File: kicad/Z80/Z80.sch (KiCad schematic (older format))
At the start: 1 part

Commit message: KiCAD Z80 testing
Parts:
- added C? (x2): C_Small, symbol Device:C_Small
- added D? (x3): LED, symbol Device:LED
- added R?: R_Small, symbol Device:R_Small
- added R? (x11): 470, symbol Device:R_Small
- added U?: HEF4093B, symbol 4xxx:HEF4093B
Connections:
- net at U?.10 (D6): now also R?.1
- net VCC: now reaches U?.11 (VCC)
- net VCC: now also C?.2
- net at U?.12 (D2): now also R?.1
- net at U?.13 (D7): now also R?.1
- net at U?.14 (D0): now also R?.1
- net at U?.15 (D1): now also R?.1
- net GND: now reaches U?.29 (GND)
- net GND: now also C?.1, C?.2, D?.1 (K), D?.1 (K), D?.1 (K), R?.2, R?.2, R?.2, R?.2, R?.2, R?.2, R?.2, R?.2
- net at U?.30 (A0): now also R?.1
- net at U?.31 (A1): now also R?.1
- net at U?.32 (A2): now also R?.1
- net CLK: now reaches U?.6 (~CLK~)
- net CLK: now also R?.1, U?.3
- net at U?.7 (D4): now also R?.1
- net at U?.8 (D3): now also R?.1
- net at U?.9 (D5): now also R?.1
- new net: C?.1, R?.2, U?.1, U?.2
- new net: D?.2 (A), R?.2 (x3)
- no-connect marks 0 -> 13
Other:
- moved on the sheet: U?

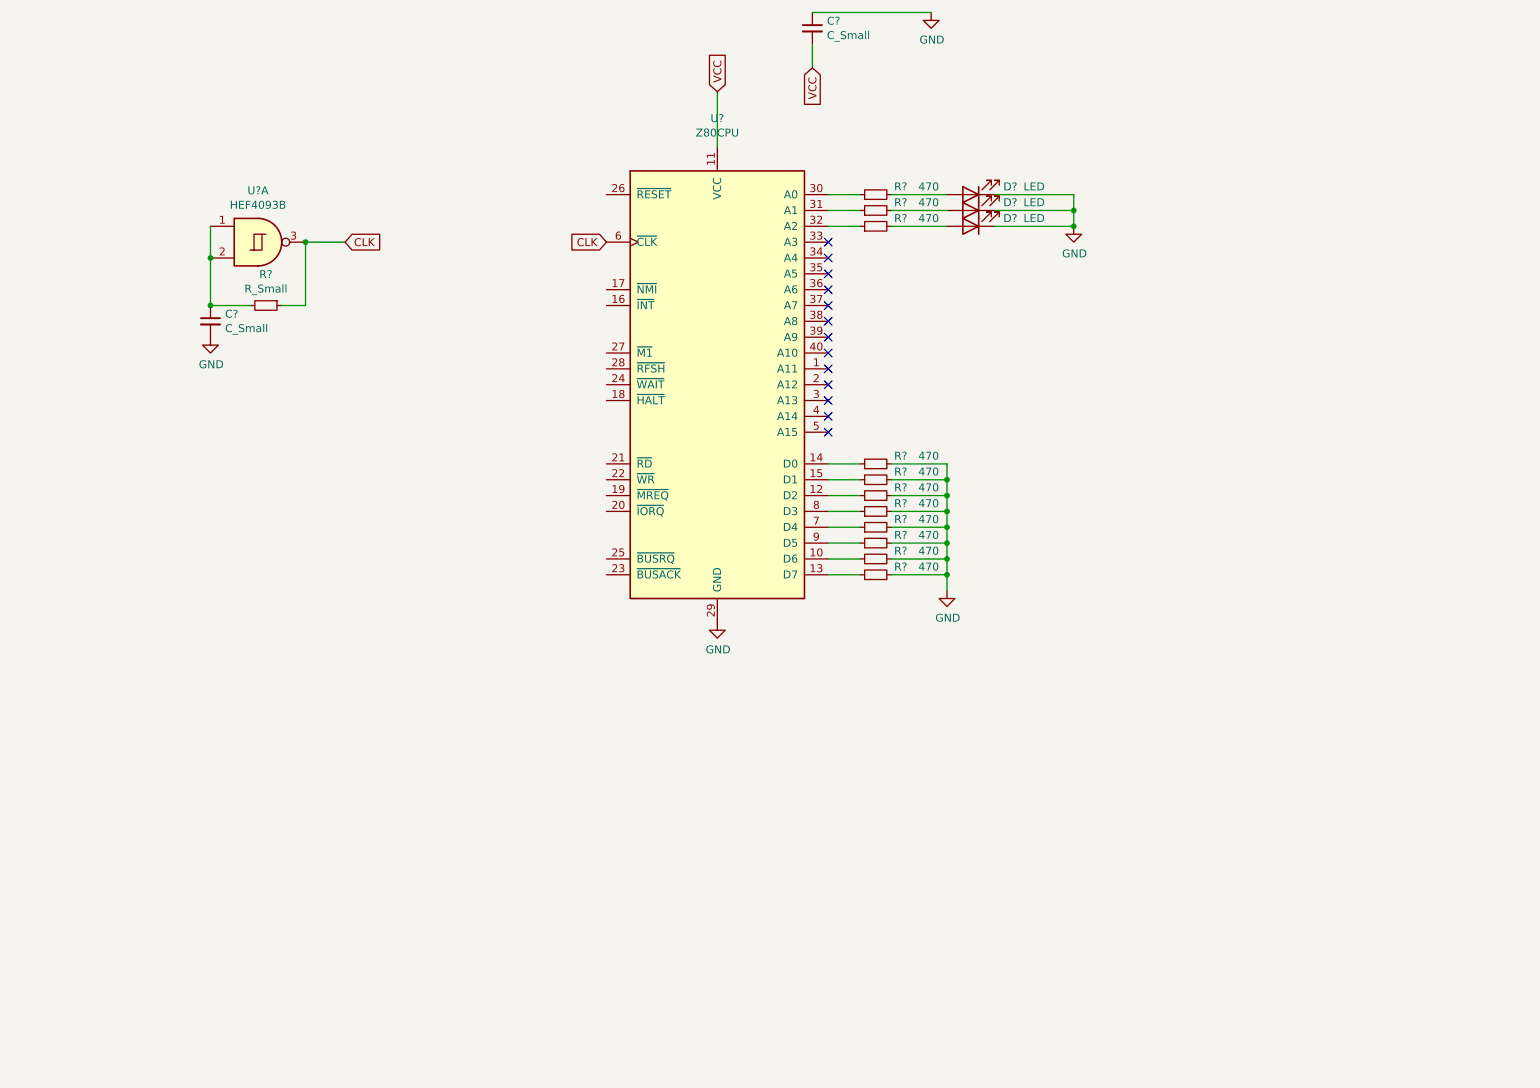
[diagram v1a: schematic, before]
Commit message: Z80 tester complete
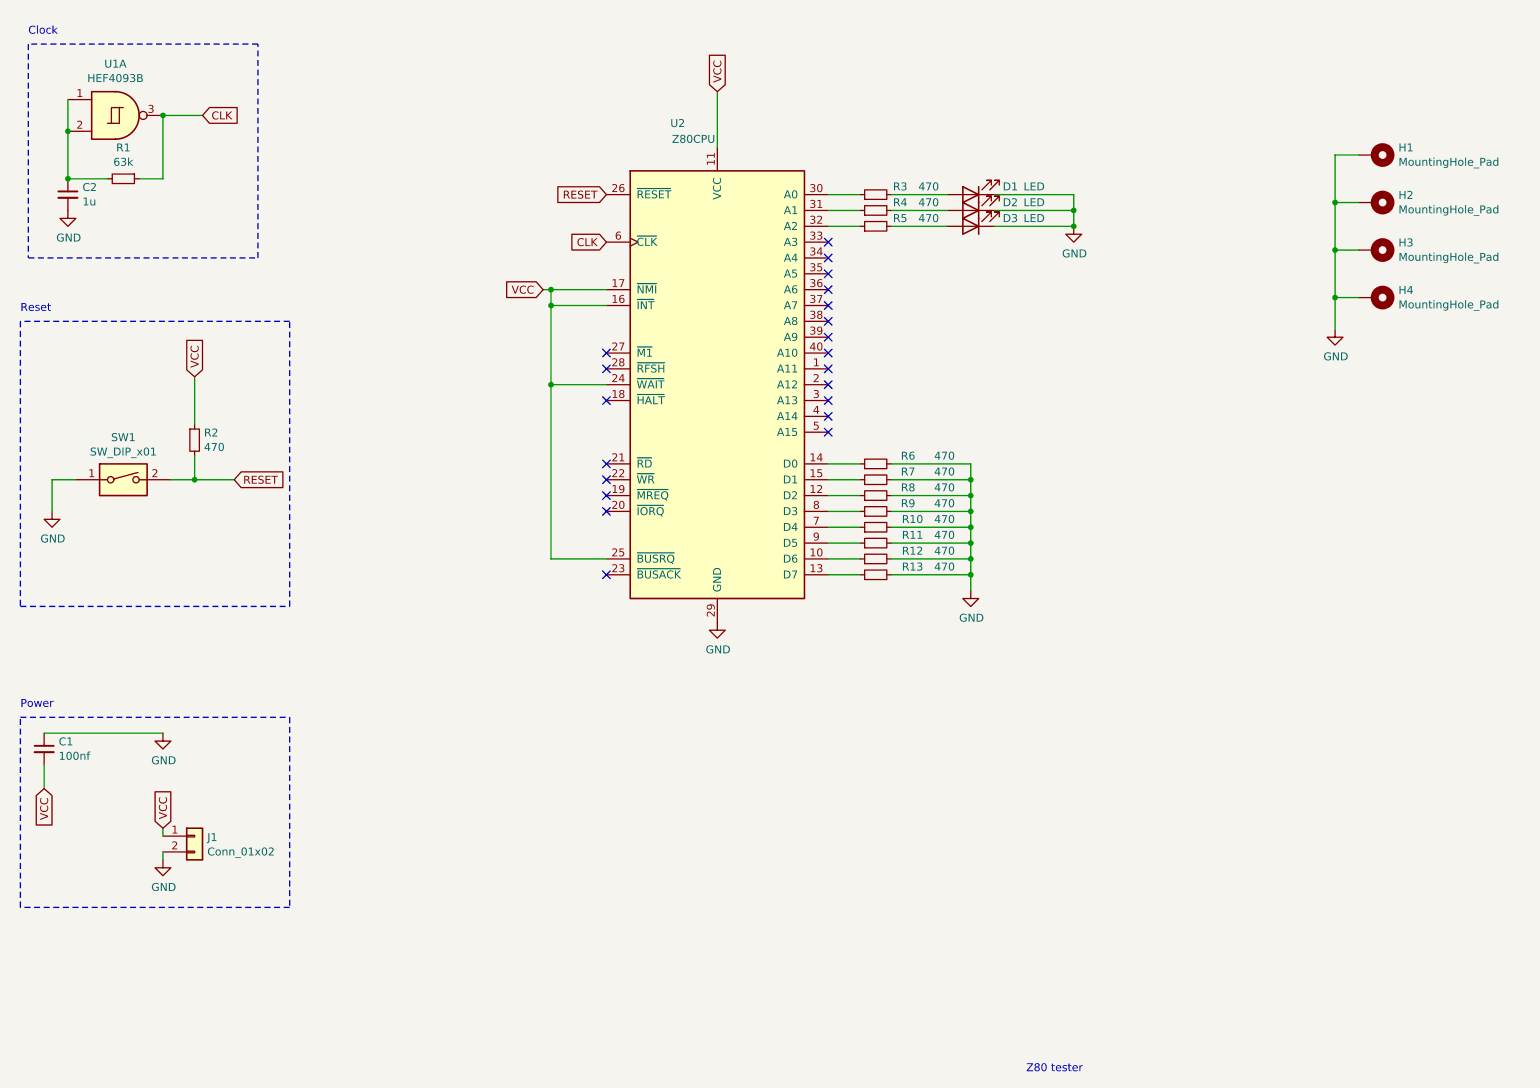
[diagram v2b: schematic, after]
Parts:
- added H1, H2, H3, H4: MountingHole_Pad, MountingHole:MountingHole_4.3mm_M4_Pad_Via, symbol Mechanical:MountingHole_Pad
- added J1: Conn_01x02, Connector_PinHeader_2.54mm:PinHeader_1x02_P2.54mm_Vertical, symbol Connector_Generic:Conn_01x02
- added R2: 470, Resistor_SMD:R_0805_2012Metric, symbol Device:R_Small
- added SW1: SW_DIP_x01, Button_Switch_SMD:SW_SPST_EVPBF, symbol Switch:SW_DIP_x01
- C1: renamed from C?; value C_Small -> 100nf; footprint (none) -> Capacitor_SMD:C_0805_2012Metric
- C2: renamed from C?; value C_Small -> 1u; footprint (none) -> Capacitor_SMD:C_0402_1005Metric
- D1, D2, D3: renamed from D?; footprint (none) -> LED_SMD:LED_0805_2012Metric
- R1: renamed from R?; value R_Small -> 63k; footprint (none) -> Resistor_SMD:R_0805_2012Metric
- R10, R11, R12, R13, R3, R4, R5, R6, R7, R8, R9: renamed from R?; footprint (none) -> Resistor_SMD:R_0805_2012Metric
- U1: renamed from U?; footprint (none) -> Package_DIP:DIP-14_W7.62mm_Socket
- U2: renamed from U?; footprint (none) -> Package_DIP:DIP-40_W15.24mm_Socket
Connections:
- net GND: now also H1.1, H2.1, H3.1, H4.1, J1.2 (Pin_2), SW1.1
- net VCC: now also U2.16 (~INT~), U2.17 (~NMI~), U2.24 (~WAIT~), U2.25 (~BUSRQ~), J1.1 (Pin_1), R2.1
- net RESET: now reaches U2.26 (~RESET~)
- net RESET: now also R2.2, SW1.2
- no-connect marks 13 -> 21
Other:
- note added: "Clock"
- note added: "Power"
- note added: "Reset"
- note added: "Z80 tester"
- moved on the sheet: C1, C2, R1, U1A

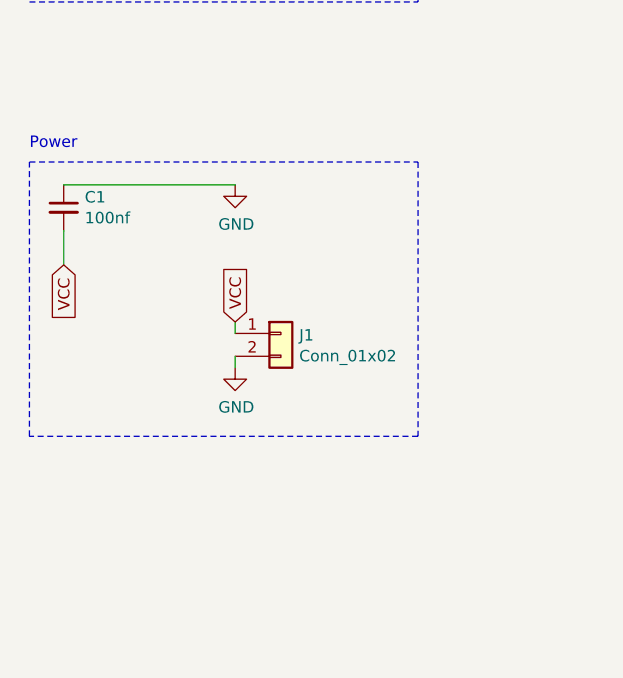
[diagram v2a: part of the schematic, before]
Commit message: add FPGA
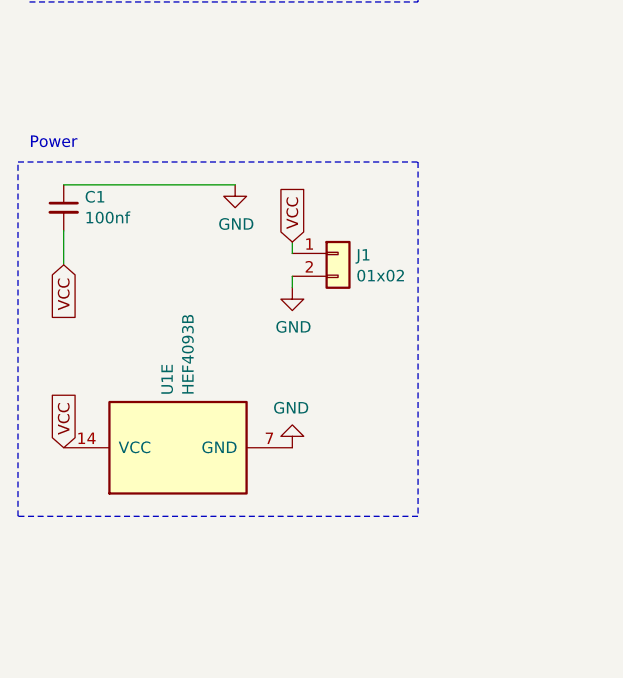
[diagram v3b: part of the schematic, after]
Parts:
- added unit 5 of U1
- C2: footprint Capacitor_SMD:C_0402_1005Metric -> Capacitor_SMD:C_0805_2012Metric
- D1, D2, D3: footprint LED_SMD:LED_0805_2012Metric -> LED_THT:LED_D5.0mm_Clear
- J1: value Conn_01x02 -> 01x02
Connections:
- net GND: now also U1.7 (GND)
- net VCC: now also U1.14 (VCC)
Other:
- moved on the sheet: J1
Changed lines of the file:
@@
 F 0 "C2" H 1442 1996 50  0000 L CNN
 F 1 "1u" H 1442 1905 50  0000 L CNN
-F 2 "Capacitor_SMD:C_0402_1005Metric" H 1350 1950 50  0001 C CNN
+F 2 "Capacitor_SMD:C_0805_2012Metric" H 1350 1950 50  0001 C CNN
 F 3 "~" H 1350 1950 50  0001 C CNN
 	1    1350 1950
@@
 F 0 "D1" H 6800 1900 50  0000 C CNN
 F 1 "LED" H 6650 1900 50  0000 C CNN
-F 2 "LED_SMD:LED_0805_2012Metric" H 7050 1950 50  0001 C CNN
+F 2 "LED_THT:LED_D5.0mm_Clear" H 7050 1950 50  0001 C CNN
 F 3 "~" H 7050 1950 50  0001 C CNN
 	1    7050 1950
@@
 F 0 "D2" H 6800 2000 50  0000 C CNN
 F 1 "LED" H 6650 2000 50  0000 C CNN
-F 2 "LED_SMD:LED_0805_2012Metric" H 7050 2050 50  0001 C CNN
+F 2 "LED_THT:LED_D5.0mm_Clear" H 7050 2050 50  0001 C CNN
 F 3 "~" H 7050 2050 50  0001 C CNN
 	1    7050 2050
@@
 F 0 "D3" H 6800 2100 50  0000 C CNN
 F 1 "LED" H 6650 2100 50  0000 C CNN
-F 2 "LED_SMD:LED_0805_2012Metric" H 7050 2150 50  0001 C CNN
+F 2 "LED_THT:LED_D5.0mm_Clear" H 7050 2150 50  0001 C CNN
 F 3 "~" H 7050 2150 50  0001 C CNN
 	1    7050 2150
@@
 L Connector_Generic:Conn_01x02 J1
 U 1 1 5EE08694
-P 2150 6000
-F 0 "J1" H 2230 5992 50  0000 L CNN
-F 1 "Conn_01x02" H 2230 5901 50  0000 L CNN
-F 2 "Connector_PinHeader_2.54mm:PinHeader_1x02_P2.54mm_Vertical" H 2150 6000 50  0001 C CNN
-F 3 "~" H 2150 6000 50  0001 C CNN
-	1    2150 6000
+P 2400 5650
+F 0 "J1" H 2480 5642 50  0000 L CNN
+F 1 "01x02" H 2480 5551 50  0000 L CNN
+F 2 "Connector_PinHeader_2.54mm:PinHeader_1x02_P2.54mm_Vertical" H 2400 5650 50  0001 C CNN
+F 3 "~" H 2400 5650 50  0001 C CNN
+	1    2400 5650
 	1    0    0    -1
 $EndComp
@@
 L power:GND #PWR04
 U 1 1 5EE09DEC
-P 1950 6150
-F 0 "#PWR04" H 1950 5900 50  0001 C CNN
-F 1 "GND" H 1955 5977 50  0000 C CNN
-F 2 "" H 1950 6150 50  0001 C CNN
-F 3 "" H 1950 6150 50  0001 C CNN
-	1    1950 6150
-	1    0    0    -1
-$EndComp
-Wire Wire Line
-	1950 6000 1950 5950
-Wire Wire Line
-	1950 6150 1950 6100
-Text GLabel 1950 5950 1    50   Input ~ 0
+P 2200 5800
+F 0 "#PWR04" H 2200 5550 50  0001 C CNN
+F 1 "GND" H 2205 5627 50  0000 C CNN
+F 2 "" H 2200 5800 50  0001 C CNN
+F 3 "" H 2200 5800 50  0001 C CNN
+	1    2200 5800
+	1    0    0    -1
+$EndComp
+Wire Wire Line
+	2200 5650 2200 5600
+Wire Wire Line
+	2200 5800 2200 5750
+Text GLabel 2200 5600 1    50   Input ~ 0
 VCC
-Wire Notes Line
-	1050 5250 2750 5250
-Wire Notes Line
-	2750 5250 2750 6450
-Wire Notes Line
-	2750 6450 1050 6450
-Wire Notes Line
-	1050 6450 1050 5250
 Text Notes 1050 5200 0    50   ~ 0
 Power
@@
 Wire Wire Line
 	9350 2600 9350 2800
+$Comp
+L 4xxx:HEF4093B U1
+U 5 1 5EDD328C
+P 1700 6500
+F 0 "U1" H 1930 6546 50  0000 L CNN
+F 1 "HEF4093B" H 1930 6455 50  0000 L CNN
+F 2 "Package_DIP:DIP-14_W7.62mm_Socket" H 1700 6500 50  0001 C CNN
+F 3 "https://assets.nexperia.com/documents/data-sheet/HEF4093B.pdf" H 1700 6500 50  0001 C CNN
+	5    1700 6500
+	0    -1   -1   0
+$EndComp
+$Comp
+L power:GND #PWR0101
+U 1 1 5EDF2C57
+P 2200 6500
+F 0 "#PWR0101" H 2200 6250 50  0001 C CNN
+F 1 "GND" H 2205 6327 50  0000 C CNN
+F 2 "" H 2200 6500 50  0001 C CNN
+F 3 "" H 2200 6500 50  0001 C CNN
+	1    2200 6500
+	-1   0    0    1
+$EndComp
+Text GLabel 1200 6500 1    50   Input ~ 0
+VCC
+Wire Notes Line
+	1000 5250 2750 5250
+Wire Notes Line
+	2750 5250 2750 6800
+Wire Notes Line
+	2750 6800 1000 6800
+Wire Notes Line
+	1000 6800 1000 5250
 $EndSCHEMATC

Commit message: Генератор курсовых работ
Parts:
- added C3: 1uF, Capacitor_SMD:C_0805_2012Metric, symbol Device:C_Small
- added C4: 100nF, Capacitor_SMD:C_0805_2012Metric, symbol Device:C_Small
- added D4: POWER, LED_SMD:LED_1206_3216Metric, symbol Device:LED_Small
- added R14: 470, Resistor_SMD:R_0805_2012Metric, symbol Device:R_Small
- C1: value 100nf -> 100nF
- C2: value 1u -> 1uF
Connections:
- net GND: now also C3.1, C4.1, D4.1 (K)
- net VCC: now also C3.2, C4.2, R14.1
- new net: D4.2 (A), R14.2
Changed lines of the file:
@@
 P 1350 1950
 F 0 "C2" H 1442 1996 50  0000 L CNN
-F 1 "1u" H 1442 1905 50  0000 L CNN
+F 1 "1uF" H 1442 1905 50  0000 L CNN
 F 2 "Capacitor_SMD:C_0805_2012Metric" H 1350 1950 50  0001 C CNN
 F 3 "~" H 1350 1950 50  0001 C CNN
@@
 U 1 1 5EDD3080
 P 1200 5450
-F 0 "C1" H 1292 5496 50  0000 L CNN
-F 1 "100nf" H 1292 5405 50  0000 L CNN
+F 0 "C1" H 1150 5600 50  0000 L CNN
+F 1 "100nF" H 1200 5300 50  0000 L CNN
 F 2 "Capacitor_SMD:C_0805_2012Metric" H 1200 5450 50  0001 C CNN
 F 3 "~" H 1200 5450 50  0001 C CNN
@@
 $EndComp
 Wire Wire Line
-	1200 5350 1950 5350
+	1200 5350 1500 5350
 $Comp
 L Device:R_Small R3
@@
 VCC
 Wire Notes Line
-	1000 5250 2750 5250
-Wire Notes Line
-	2750 5250 2750 6800
-Wire Notes Line
-	2750 6800 1000 6800
-Wire Notes Line
-	1000 6800 1000 5250
+	2880 5260 2880 6810
+$Comp
+L Device:C_Small C3
+U 1 1 5EFCCBD6
+P 1500 5450
+F 0 "C3" H 1450 5605 50  0000 L CNN
+F 1 "1uF" H 1450 5300 50  0000 L CNN
+F 2 "Capacitor_SMD:C_0805_2012Metric" H 1500 5450 50  0001 C CNN
+F 3 "~" H 1500 5450 50  0001 C CNN
+	1    1500 5450
+	1    0    0    -1
+$EndComp
+Wire Wire Line
+	1200 5550 1500 5550
+Connection ~ 1200 5550
+Connection ~ 1500 5350
+Connection ~ 1500 5550
+Wire Wire Line
+	1500 5350 1700 5350
+$Comp
+L Device:C_Small C4
+U 1 1 5EFE2DEC
+P 1700 5450
+F 0 "C4" H 1650 5610 50  0000 L CNN
+F 1 "100nF" H 1620 5300 50  0000 L CNN
+F 2 "Capacitor_SMD:C_0805_2012Metric" H 1700 5450 50  0001 C CNN
+F 3 "~" H 1700 5450 50  0001 C CNN
+	1    1700 5450
+	1    0    0    -1
+$EndComp
+Connection ~ 1700 5350
+Wire Wire Line
+	1700 5350 1950 5350
+Wire Wire Line
+	1500 5550 1700 5550
+$Comp
+L Device:LED_Small D4
+U 1 1 5EFEDAD3
+P 2600 6140
+F 0 "D4" H 2600 6375 50  0000 C CNN
+F 1 "POWER" H 2600 6284 50  0000 C CNN
+F 2 "LED_SMD:LED_1206_3216Metric" V 2600 6140 50  0001 C CNN
+F 3 "~" V 2600 6140 50  0001 C CNN
+	1    2600 6140
+	-1   0    0    -1
+$EndComp
+$Comp
+L Device:R_Small R14
+U 1 1 5EFF059F
+P 2160 6140
+F 0 "R14" V 2210 5940 50  0000 L CNN
+F 1 "470" V 2210 5740 50  0000 L CNN
+F 2 "Resistor_SMD:R_0805_2012Metric" H 2160 6140 50  0001 C CNN
+F 3 "~" H 2160 6140 50  0001 C CNN
+	1    2160 6140
+	0    -1   -1   0
+$EndComp
+Text GLabel 2060 6140 0    50   Input ~ 0
+VCC
+$Comp
+L power:GND #PWR0102
+U 1 1 5EFFC30A
+P 2770 6220
+F 0 "#PWR0102" H 2770 5970 50  0001 C CNN
+F 1 "GND" H 2775 6047 50  0000 C CNN
+F 2 "" H 2770 6220 50  0001 C CNN
+F 3 "" H 2770 6220 50  0001 C CNN
+	1    2770 6220
+	1    0    0    -1
+$EndComp
+Wire Wire Line
+	2260 6140 2500 6140
+Wire Wire Line
+	2700 6140 2770 6140
+Wire Wire Line
+	2770 6140 2770 6220
+Wire Notes Line
+	1000 5250 2880 5250
+Wire Notes Line
+	1000 6810 2880 6810
+Wire Notes Line
+	1000 5250 1000 6810
 $EndSCHEMATC
